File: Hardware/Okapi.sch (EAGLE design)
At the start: 214 parts, among them IC1 ATMEGA1284M, J1 CONN_82.54_SCREW, J3 CONN_42.54_SCREW, J4 CONN_82.54_SCREW, Q1 DMG3404, Q2 DMG3404, Q3 FDN360P, Q4 2N7002, Q5 FDN360P, Q6 DMG3404, Q7 2N7002, Q8 2N7002, U1 TLV61220DBV, U10 TPS22917DBV, U11 SN74AUP1G04YFP, U12 SN74AUP1G04YFP, U13 SN74AUP1G04YFP, U14 SN74AUP2G08DQE, U15 SN74AUP2G08DQE, U16 SN74AUP2G08DQE, U17 MIC2544MSOP, U18 MIC2544MSOP, U19 MIC2544MSOP, U2 TPS62822DLC, U20 MIC2544MSOP, U21 TPS22917DBV, U22 TPS22917DBV, U23 FT231X-Q, U24 SN74LVC1G3157DRL, U25 SN74AUP3G34DCU, U26 TXS0102DQM, U27 TXS0104RGY, U28 TCA9406DCU, U29 TXS0104RGY, U3 TPS61032RSA, U30 MCP4726A2SOT-23, U31 BME280, U32 ADS1115, U33 ADS1115, U34 INA211DCK, U35 INA213DCK, U36 TCA9406DCU, U37 TLV3691DCK, U38 TS5A21366RSE, U39 MIC94094C6, U40 SN74AHC1G86DCK, U41 MCP23018QFN, U42 TXS0104RGY, U5 BQ2980RUG, U6 TPS2105, U7 LTC4412S6, U8 TPL5111DDC, U9 TPS79733

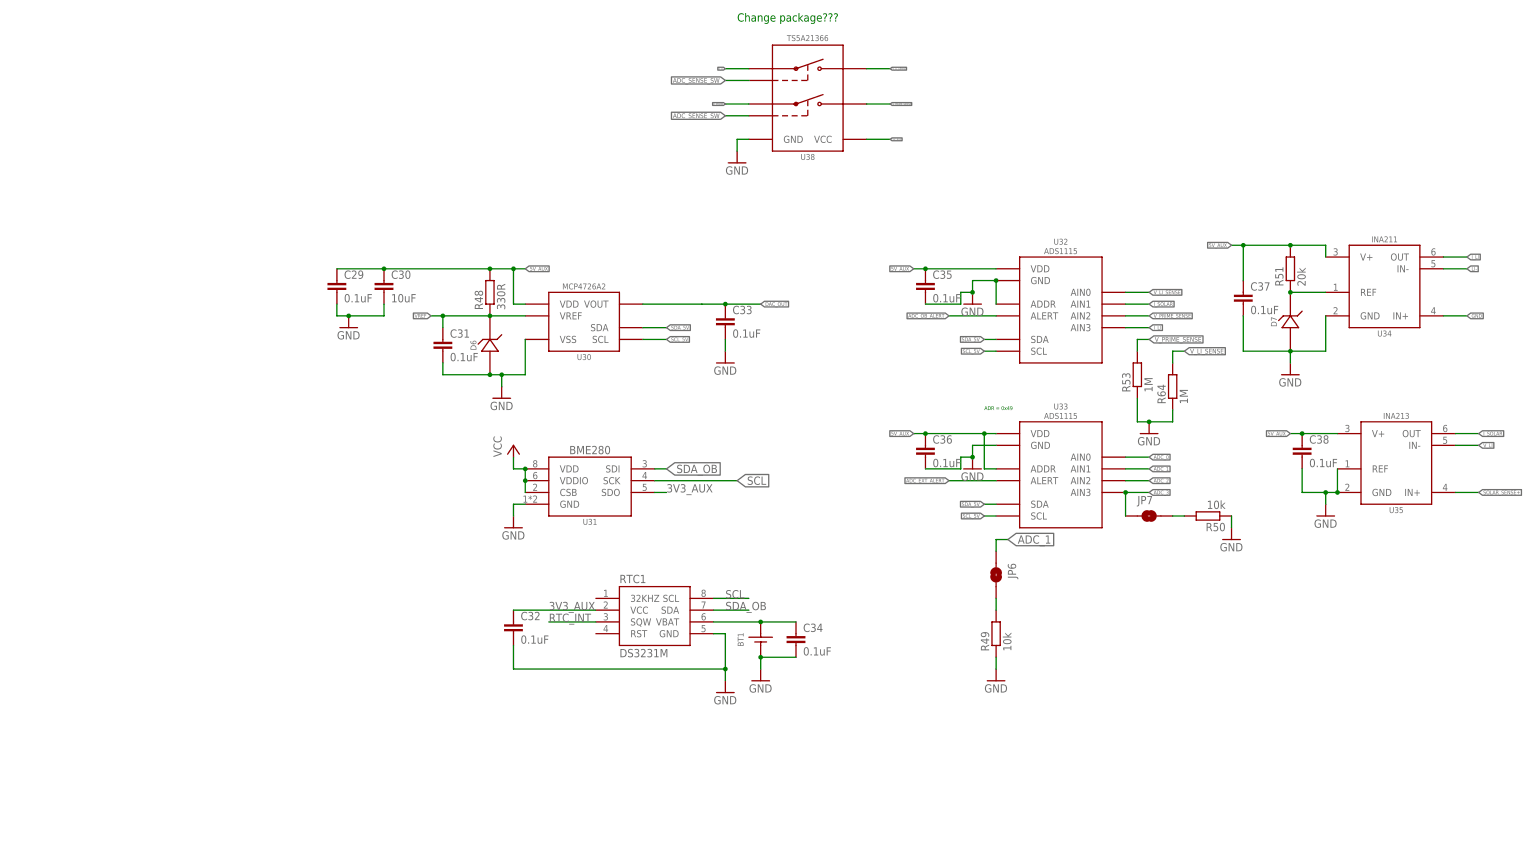
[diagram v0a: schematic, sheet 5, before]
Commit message: Updated layout
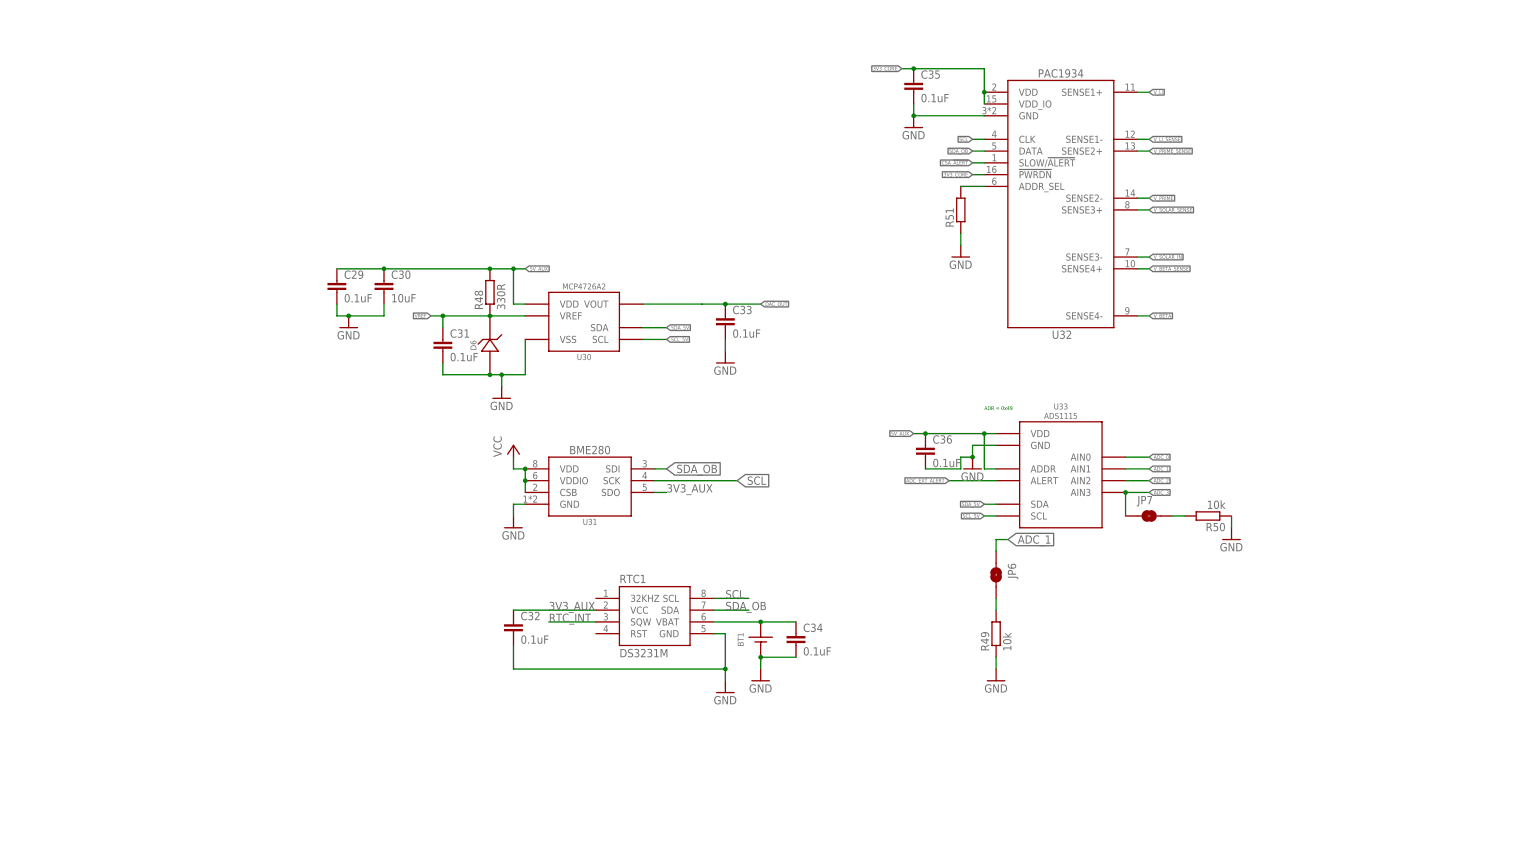
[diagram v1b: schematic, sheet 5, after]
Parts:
- removed C37, C38: 0.1uF, bschulz_passives:C-EU0.1UFC0402
- removed D7: (no value), bschulz:LM40402.5
- removed R18: 50m, bschulz_passives:R-EU_0.05R0805
- removed R53, R64: 1M, bschulz_passives:R-EU_1MR0402
- removed U34: INA211DCK, bschulz:INA211DCK
- removed U35: INA213DCK, bschulz:INA213DCK
- removed U38: TS5A21366RSE, bschulz:TS5A21366RSE
- added R72, R73, R74, R75: (no value), bschulz_passives:R-EU_R0805
- R51: value 20k -> (none); device bschulz_passives:R-EU_20KR0603 -> bschulz_passives:R-EU_R0402
- U32: value ADS1115 -> PAC1934QFN; device bschulz:ADS1115 -> bschulz:PAC1934QFN
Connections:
- removed net I_LI: U32.AIN3, U34.OUT
- removed net I_SOLAR: U32.AIN1, U35.OUT
- removed net SOLAR_SENSE+: L4.2, R18.1, U35.IN+, U4.SENSE
- new net CSA_!ALERT: U32.SLOW/!ALERT, U41.GPB4
- new net V_BETA_SENSE: D9.C, Q5.S, R75.1, U32.SENSE4+
- new net V_SOLAR_SENSE: D1.C, R74.1, U32.SENSE3+
- net 3V3_CORE: now also C35.1, U32.!PWRDN, U32.VDD, U32.VDD_IO
- net 5V_AUX: no longer C35.1, C37.1, C38.1, R51.2, U32.VDD, U34.V+, U35.V+, U38.VCC
- net ADC_OB_ALERT: no longer U32.ALERT, U41.GPB4
- net ADC_SENSE_SW: no longer U38.S1, U38.S2
- net GND: now also R51.1; no longer C37.2, C38.2, D7.A, R53.1, R64.1, U32.ADDR, U34.GND, U34.IN+, U35.GND, U35.REF, U38.GND
- net LI-: no longer U34.IN-
- net N$21: now also R51.2, U32.ADDR_SEL; no longer D7.C, R51.1, U34.REF
- net SCL: now also U32.CLK
- net SCL_5V: no longer U32.SCL
- net SDA_5V: no longer U32.SDA
- net SDA_OB: now also U32.DATA
- net V_BETA: now also R75.2, U32.SENSE4-; no longer D9.C, Q5.S
- net V_LI: now also L4.2, R72.2, U32.SENSE1+, U4.SENSE; no longer Q2.S, R18.2, U35.IN-, U38.A1
- net V_LI_SENSE: now also Q2.S, R72.1, U32.SENSE1-; no longer R64.2, U32.AIN0, U38.B1
- net V_PRIME: now also R73.2, U32.SENSE2-; no longer J5.2, U38.A2
- net V_PRIME_SENSE: now also J5.2, R73.1, U32.SENSE2+; no longer R53.2, U32.AIN2, U38.B2
- net V_SOLAR_IN: now also R74.2, U32.SENSE3-; no longer D1.C
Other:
- note removed: "Change package???"
- moved on the sheet: C35, D1, Q5, R15, R51

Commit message: CSA layout
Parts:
- removed R60: 100k, bschulz_passives:R-EU_100KR0402
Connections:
- removed net ADC_OB_ALERT: R60.1
- net 5V_AUX: no longer R60.2
- net V_BETA: now also U32.SENSE3-; no longer U32.SENSE4-
- net V_BETA_SENSE: now also U32.SENSE3+; no longer U32.SENSE4+
- net V_LI: now also U32.SENSE2+; no longer U32.SENSE1+
- net V_LI_SENSE: now also U32.SENSE2-; no longer U32.SENSE1-
- net V_PRIME: now also U32.SENSE1-; no longer U32.SENSE2-
- net V_PRIME_SENSE: now also U32.SENSE1+; no longer U32.SENSE2+
- net V_SOLAR_IN: now also U32.SENSE4-; no longer U32.SENSE3-
- net V_SOLAR_SENSE: now also U32.SENSE4+; no longer U32.SENSE3+
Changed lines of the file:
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@@
 <part name="R58" library="bschulz_passives" deviceset="R-EU_" device="R0402" technology="100K" value="100k"/>
 <part name="R59" library="bschulz_passives" deviceset="R-EU_" device="R0402" technology="1M" value="1M"/>
-<part name="R60" library="bschulz_passives" deviceset="R-EU_" device="R0402" technology="100K" value="100k"/>
 <part name="R61" library="bschulz_passives" deviceset="R-EU_" device="R0402" technology="100K" value="100k"/>
 <part name="GND31" library="supply1" library_urn="urn:adsk.eagle:library:371" deviceset="GND" device=""/>
@@
 <net name="V_LI" class="0">
 <segment>
-<pinref part="U32" gate="G$1" pin="SENSE1+"/>
-<wire x1="142.24" y1="144.78" x2="144.78" y2="144.78" width="0.1524" layer="91"/>
-<label x="144.78" y="144.78" size="0.8128" layer="95" xref="yes"/>
-</segment>
-</net>
-<net name="V_LI_SENSE" class="0">
-<segment>
-<pinref part="U32" gate="G$1" pin="SENSE1-"/>
-<wire x1="142.24" y1="134.62" x2="144.78" y2="134.62" width="0.1524" layer="91"/>
-<label x="144.78" y="134.62" size="0.8128" layer="95" xref="yes"/>
-</segment>
-</net>
-<net name="V_PRIME_SENSE" class="0">
-<segment>
 <pinref part="U32" gate="G$1" pin="SENSE2+"/>
 <wire x1="142.24" y1="132.08" x2="144.78" y2="132.08" width="0.1524" layer="91"/>
@@
 <net name="V_PRIME" class="0">
 <segment>
-<pinref part="U32" gate="G$1" pin="SENSE2-"/>
-<wire x1="142.24" y1="121.92" x2="144.78" y2="121.92" width="0.1524" layer="91"/>
-<label x="144.78" y="121.92" size="0.8128" layer="95" xref="yes"/>
+<pinref part="U32" gate="G$1" pin="SENSE1-"/>
+<wire x1="142.24" y1="134.62" x2="144.78" y2="134.62" width="0.1524" layer="91"/>
+<label x="144.78" y="134.62" size="0.8128" layer="95" xref="yes"/>
 </segment>
 </net>
 <net name="V_SOLAR_SENSE" class="0">
 <segment>
-<pinref part="U32" gate="G$1" pin="SENSE3+"/>
-<wire x1="142.24" y1="119.38" x2="144.78" y2="119.38" width="0.1524" layer="91"/>
-<label x="144.78" y="119.38" size="0.8128" layer="95" xref="yes"/>
-</segment>
-</net>
-<net name="V_SOLAR_IN" class="0">
-<segment>
-<pinref part="U32" gate="G$1" pin="SENSE3-"/>
-<wire x1="142.24" y1="109.22" x2="144.78" y2="109.22" width="0.1524" layer="91"/>
-<label x="144.78" y="109.22" size="0.8128" layer="95" xref="yes"/>
-</segment>
-</net>
-<net name="V_BETA_SENSE" class="0">
-<segment>
 <pinref part="U32" gate="G$1" pin="SENSE4+"/>
 <wire x1="142.24" y1="106.68" x2="144.78" y2="106.68" width="0.1524" layer="91"/>
@@
 <net name="V_BETA" class="0">
 <segment>
-<pinref part="U32" gate="G$1" pin="SENSE4-"/>
-<wire x1="142.24" y1="96.52" x2="144.78" y2="96.52" width="0.1524" layer="91"/>
-<label x="144.78" y="96.52" size="0.8128" layer="95" xref="yes"/>
+<pinref part="U32" gate="G$1" pin="SENSE3-"/>
+<wire x1="142.24" y1="109.22" x2="144.78" y2="109.22" width="0.1524" layer="91"/>
+<label x="144.78" y="109.22" size="0.8128" layer="95" xref="yes"/>
 </segment>
 </net>
@@
 </segment>
 </net>
+<net name="V_SOLAR_IN" class="0">
+<segment>
+<pinref part="U32" gate="G$1" pin="SENSE4-"/>
+<wire x1="142.24" y1="96.52" x2="144.78" y2="96.52" width="0.1524" layer="91"/>
+<label x="144.78" y="96.52" size="0.8128" layer="95" xref="yes"/>
+</segment>
+</net>
+<net name="V_BETA_SENSE" class="0">
+<segment>
+<pinref part="U32" gate="G$1" pin="SENSE3+"/>
+<wire x1="142.24" y1="119.38" x2="144.78" y2="119.38" width="0.1524" layer="91"/>
+<label x="144.78" y="119.38" size="0.8128" layer="95" xref="yes"/>
+</segment>
+</net>
+<net name="V_LI_SENSE" class="0">
+<segment>
+<pinref part="U32" gate="G$1" pin="SENSE2-"/>
+<wire x1="142.24" y1="121.92" x2="144.78" y2="121.92" width="0.1524" layer="91"/>
+<label x="144.78" y="121.92" size="0.8128" layer="95" xref="yes"/>
+</segment>
+</net>
+<net name="V_PRIME_SENSE" class="0">
+<segment>
+<pinref part="U32" gate="G$1" pin="SENSE1+"/>
+<wire x1="142.24" y1="144.78" x2="144.78" y2="144.78" width="0.1524" layer="91"/>
+<label x="144.78" y="144.78" size="0.8128" layer="95" xref="yes"/>
+</segment>
+</net>
 </nets>
 </sheet>
@@
 <attribute name="VALUE" x="188.722" y="34.29" size="1.778" layer="96" rot="R90"/>
 </instance>
-<instance part="R60" gate="G$1" x="157.48" y="20.32" smashed="yes" rot="R90">
-<attribute name="NAME" x="155.9814" y="16.51" size="1.778" layer="95" rot="R90"/>
-<attribute name="VALUE" x="160.782" y="16.51" size="1.778" layer="96" rot="R90"/>
-</instance>
 <instance part="R61" gate="G$1" x="172.72" y="30.48" smashed="yes" rot="R90">
 <attribute name="NAME" x="171.2214" y="26.67" size="1.778" layer="95" rot="R90"/>
@@
 </segment>
 </net>
-<net name="ADC_OB_ALERT" class="0">
-<segment>
-<label x="210.82" y="15.24" size="0.8128" layer="95" xref="yes"/>
-<pinref part="R60" gate="G$1" pin="1"/>
-<wire x1="210.82" y1="15.24" x2="157.48" y2="15.24" width="0.1524" layer="91"/>
-</segment>
-</net>
 <net name="FEATHER_EN" class="0">
 <segment>
@@
 <pinref part="R58" gate="G$1" pin="2"/>
 <wire x1="165.1" y1="27.94" x2="165.1" y2="45.72" width="0.1524" layer="91"/>
-<pinref part="R60" gate="G$1" pin="2"/>
-<wire x1="157.48" y1="25.4" x2="157.48" y2="45.72" width="0.1524" layer="91"/>
 <wire x1="165.1" y1="45.72" x2="157.48" y2="45.72" width="0.1524" layer="91"/>
 <label x="157.48" y="45.72" size="0.8128" layer="95" rot="R180" xref="yes"/>

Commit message: Design updates toward v1.0
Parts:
- removed USB1: MICRO_USB_LONGPADS, bschulz:MICRO_USB_LONGPADS
- added C37, C38, C46, C47, C48, C50, C57: 0.1uF, bschulz_passives:C-EU0.1UFC0402
- added D10, D13, D16: LEDGREEN0603, bschulz:LEDGREEN0603
- added D11, D14, D17: LEDYELLOW0603, bschulz:LEDYELLOW0603
- added D12, D18: LEDRED0603, bschulz:LEDRED0603
- added D7: CLVBA-FKA, bschulz:CLVBA-FKA
- added F2: (no value), bschulz:PPTC1.5A
- added J10: (no value), microbuilder:USB_C
- added J9: B_SERIES_M.2EKEY_NOPROG, bschulz:B_SERIES_M.2EKEY_NOPROG
- added R18: 100k, bschulz_passives:R-EU_100KR0402
- added R53, R60, R64, R76, R77, R78, R79, R80: 220R, bschulz_passives:R-EU_220R0402
- added R81, R82, R83: 5.6k, bschulz_passives:R-EU_5.6KR0402
- added R84, R85: (no value), bschulz_passives:R-EU_5.1KR0402
- added U34: TXS0102DQM, bschulz:TXS0102DQM
- added U35: MB85RC, bschulz:MB85RC
- added U38: MLX90393, bschulz:MLX90393
- added U43: BMA456, bschulz:BMA456
- added U44: VEML6030, bschulz:VEML6030
- added U45: PCA9634QFN, bschulz:PCA9634QFN
- added USB2: USB_MICROVERT, bschulz:USB_MICROVERT
- F1: value PPTC1.5A -> (none)
- L1: device bschulz:INDUCTOR1008 -> bschulz:INDUCTOR_1008
- L2: device bschulz:INDUCTORXHMI_6.65X6.45 -> bschulz:INDUCTOR_XHMI_6.65X6.45
- L3: device bschulz:INDUCTORLQS_3X3 -> bschulz:INDUCTOR_LQS_3X3
- L4: device bschulz:INDUCTORMAIA_4.1X4.1 -> bschulz:INDUCTOR_MAIA_4.1X4.1
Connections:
- removed net ADC_SENSE_SW: IC1.(PCINT8/XCK0/T0)PB0
- removed net N$1: USB1.BODY
- removed net N$48: C24.2, R35.2, USB1.D+
- removed net N$49: C23.2, R34.2, USB1.D-
- new net !LED_EN: IC1.(PCINT8/XCK0/T0)PB0, R18.1, U45.!OE
- new net 3V3_FEATHER: C37.1, D7.ANODE, MS1.3V, U34.EN, U34.VB
- new net BLUE: J9.RGB_BLUE, R83.2
- new net BSOM_VUSB: F2.1, J9.VBUS, USB2.VDD
- new net CC1: J10.CC1, R85.2
- new net CC2: J10.CC2, R84.2
- new net D+: C24.2, J10.D+, R35.2
- new net D-: C23.2, J10.D-, R34.2
- new net GREEN: J9.RGB_GREEN, R82.2
- new net N$25: D10.CATHODE, U45.LED0
- new net N$67: D11.CATHODE, U45.LED1
- new net N$70: D12.CATHODE, U45.LED2
- new net N$71: D13.CATHODE, U45.LED3
- new net N$72: D14.CATHODE, U45.LED4
- new net N$73: D16.CATHODE, U45.LED5
- new net N$74: D17.CATHODE, U45.LED6
- new net N$75: D18.CATHODE, U45.LED7
- new net N$76: D10.ANODE, R53.1
- new net N$77: D11.ANODE, R60.1
- new net N$78: D12.ANODE, R64.1
- new net N$79: D13.ANODE, R76.1
- new net N$80: D14.ANODE, R77.1
- new net N$81: D16.ANODE, R78.1
- new net N$82: D17.ANODE, R79.1
- new net N$83: D18.ANODE, R80.1
- new net N$84: D7.RED_CATH, R81.1
- new net N$85: D7.GREEN_CATH, R82.1
- new net N$86: D7.BLUE_CATH, R83.1
- new net PD+: J9.USB_P, USB2.D+
- new net PD-: J9.USB_N, USB2.D-
- new net RED: J9.RGB_RED, R81.2
- new net SBU1: J10.SBU1
- new net SBU2: J10.SBU2
- new net SCL_FEATHER: J9.SCL, MS1.GPIOSCL, U34.B2
- new net SDA_FEATHER: J9.SDA, MS1.GPIOSDA, U34.B1
- new net SENSOR_INT: U43.INT
- net 3V3_AUX: now also C38.1, C46.1, C47.1, C48.1, C57.1, U38.MS/CS, U38.VDD, U38.VDD_IO, U43.VCC, U44.ADDR, U44.VDD
- net 3V3_CORE: now also C50.1, R18.2, R53.2, R60.2, R64.2, R76.2, R77.2, R78.2, R79.2, R80.2, U34.VA, U35.VDD, U45.A1, U45.A4, U45.A6, U45.VDD
- net 5V_AUX: now also F2.2
- net FEATHER_BAT: now also J9.VCC@2, J9.VCC@4, J9.VCC@6, J9.VCC@8
- net FEATHER_CTS: now also J9.CTS
- net FEATHER_GPIO: now also J9.ADC5
- net FEATHER_RTS: now also J9.RTS
- net GND: now also C37.2, C38.2, C46.2, C47.2, C48.2, C50.2, C57.2, J10.GND, J9.AGND@39, J9.AGND@49, J9.GND@1, J9.GND@15, J9.GND@21, J9.GND@3, J9.GND@5, J9.GND@56, J9.GND@7, J9.GND@76, J9.GND@77, J9.GND@9, R84.1, R85.1, U34.GND, U35.A0, U35.A1, U35.A2, U35.VSS, U35.WP, U38.A0, U38.A1, U38.VSS, U43.GND, U44.GND, U45.A0, U45.A2, U45.A3, U45.A5, U45.VSS, USB2.GND; no longer USB1.GND
- net MISO: now also J9.MISO
- net MOSI_BUF: now also J9.MOSI
- net RST_TRIG: now also J9.PWM0
- net RX: now also J9.TX
- net SCK_BUF: now also J9.SCK
- net SCL: now also U34.A2, U35.SCL, U38.SCL/SCLK, U43.SCL, U44.SCL, U45.SCL; no longer MS1.GPIOSCL
- net SDA_OB: now also U34.A1, U35.SDA, U38.SDA/MOSI, U43.SDA, U44.SDA, U45.SDA; no longer MS1.GPIOSDA
- net TX: now also J9.RX
- net VUSB: now also J10.VBUS; no longer USB1.VDD
- net WD_DONE: now also J9.ADC3
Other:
- note added: "ADR = 0x48"
- note added: "ADR: 0x50"
- note added: "ADR: 0x52"
- note added: "ADR=0x0C"
- note added: "ADR=0x10 - FLEX"
- note added: "ADR=0x18"
- note added: "ADR=0x20"
- note added: "ADR=0x62"
- note added: "ADR=0x68"
- note added: "ADR=0x77"
- note added: "Select address!"

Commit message: Continued design updates
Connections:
- net 3V3_FEATHER: now also J9.3V3@10, J9.3V3@12
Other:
- moved on the sheet: F2
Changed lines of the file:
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@@
 <attribute name="VALUE" x="24.13" y="194.818" size="1.778" layer="96"/>
 </instance>
-<instance part="F2" gate="G$1" x="172.72" y="223.52" smashed="yes">
-<attribute name="NAME" x="174.625" y="226.695" size="1.778" layer="95" font="vector" align="bottom-center"/>
-<attribute name="VALUE" x="173.99" y="220.726" size="1.778" layer="96" font="vector" align="top-center"/>
+<instance part="F2" gate="G$1" x="175.26" y="223.52" smashed="yes">
+<attribute name="NAME" x="177.165" y="226.695" size="1.778" layer="95" font="vector" align="bottom-center"/>
+<attribute name="VALUE" x="176.53" y="220.726" size="1.778" layer="96" font="vector" align="top-center"/>
 </instance>
 <instance part="USB2" gate="G$1" x="68.58" y="228.6" smashed="yes">
@@
 <segment>
 <pinref part="F2" gate="G$1" pin="2"/>
-<wire x1="180.34" y1="223.52" x2="182.88" y2="223.52" width="0.1524" layer="91"/>
-<label x="182.88" y="223.52" size="0.8128" layer="95" xref="yes"/>
+<wire x1="182.88" y1="223.52" x2="185.42" y2="223.52" width="0.1524" layer="91"/>
+<label x="185.42" y="223.52" size="0.8128" layer="95" xref="yes"/>
 </segment>
 </net>
@@
 <label x="2.54" y="205.74" size="0.8128" layer="95" rot="R180" xref="yes"/>
 </segment>
+<segment>
+<pinref part="J9" gate="U1" pin="3V3@10"/>
+<pinref part="J9" gate="U1" pin="3V3@12"/>
+<wire x1="152.4" y1="231.14" x2="152.4" y2="228.6" width="0.1524" layer="91"/>
+<wire x1="152.4" y1="231.14" x2="154.94" y2="231.14" width="0.1524" layer="91"/>
+<junction x="152.4" y="231.14"/>
+<label x="154.94" y="231.14" size="0.8128" layer="95" xref="yes"/>
+</segment>
 </net>
 <net name="SCL_FEATHER" class="0">
@@
 <pinref part="J9" gate="U1" pin="VBUS"/>
 <pinref part="F2" gate="G$1" pin="1"/>
-<wire x1="152.4" y1="223.52" x2="167.64" y2="223.52" width="0.1524" layer="91"/>
-<wire x1="167.64" y1="223.52" x2="167.64" y2="231.14" width="0.1524" layer="91"/>
-<junction x="167.64" y="223.52"/>
-<wire x1="167.64" y1="231.14" x2="175.26" y2="231.14" width="0.1524" layer="91"/>
+<wire x1="152.4" y1="223.52" x2="170.18" y2="223.52" width="0.1524" layer="91"/>
+<wire x1="170.18" y1="223.52" x2="170.18" y2="231.14" width="0.1524" layer="91"/>
+<junction x="170.18" y="223.52"/>
+<wire x1="170.18" y1="231.14" x2="175.26" y2="231.14" width="0.1524" layer="91"/>
 <label x="175.26" y="231.14" size="0.8128" layer="95" xref="yes"/>
 </segment>
